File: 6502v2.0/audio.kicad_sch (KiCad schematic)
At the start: 24 parts, among them J16 AudioPlug4, U13 PSG_AY-3-8910, U14 PSG_AY-3-8910

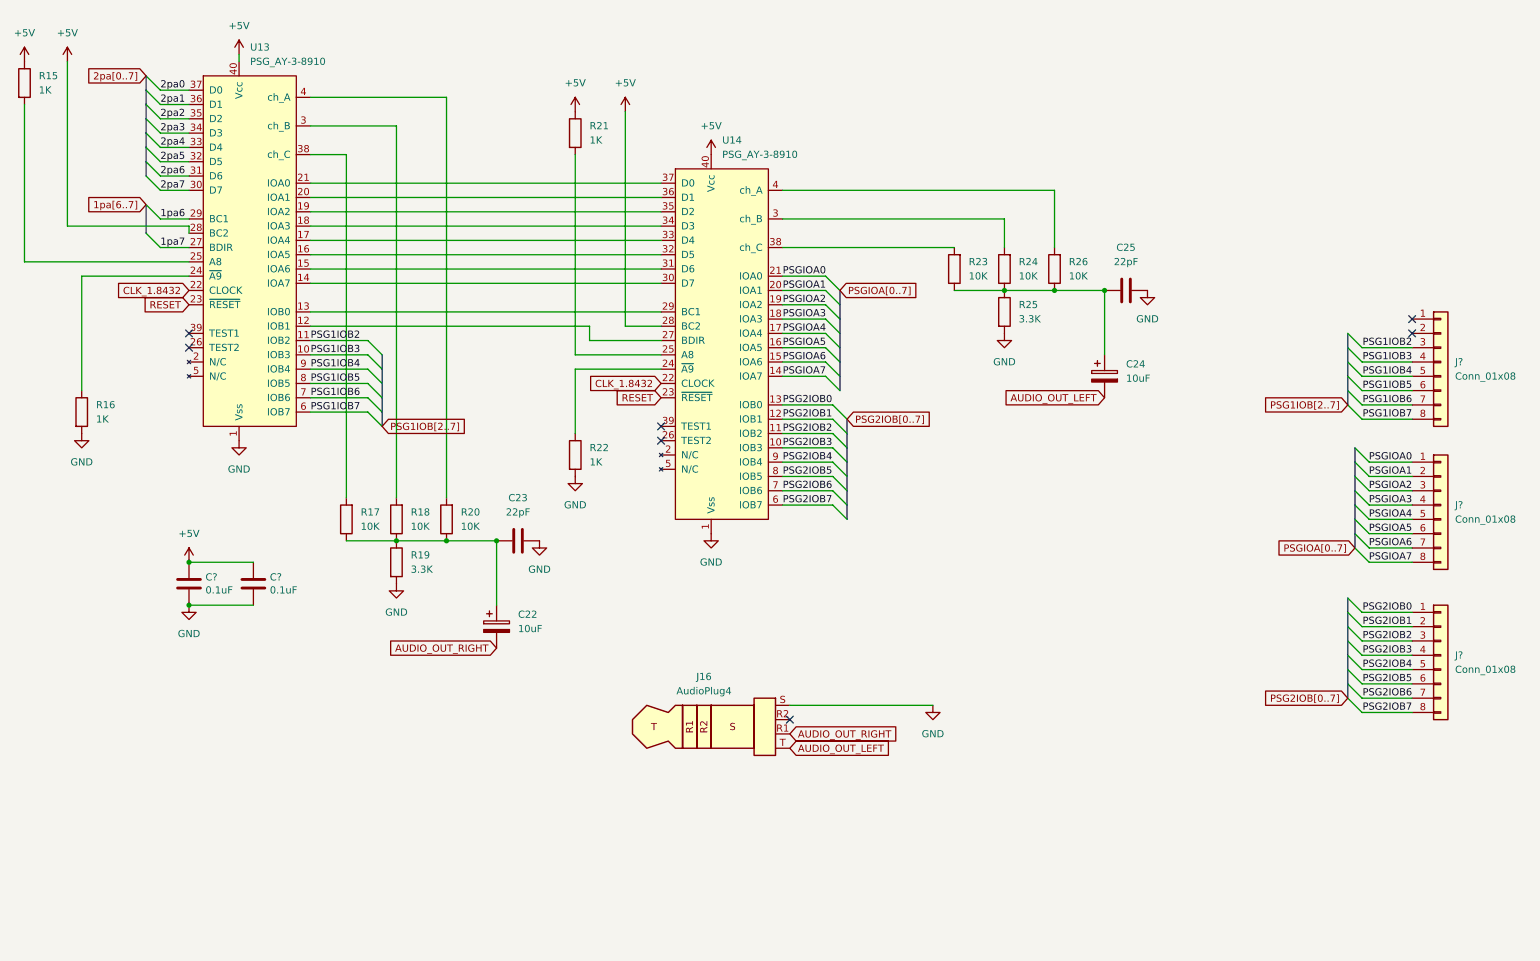
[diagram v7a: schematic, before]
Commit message: worked on new sound interface
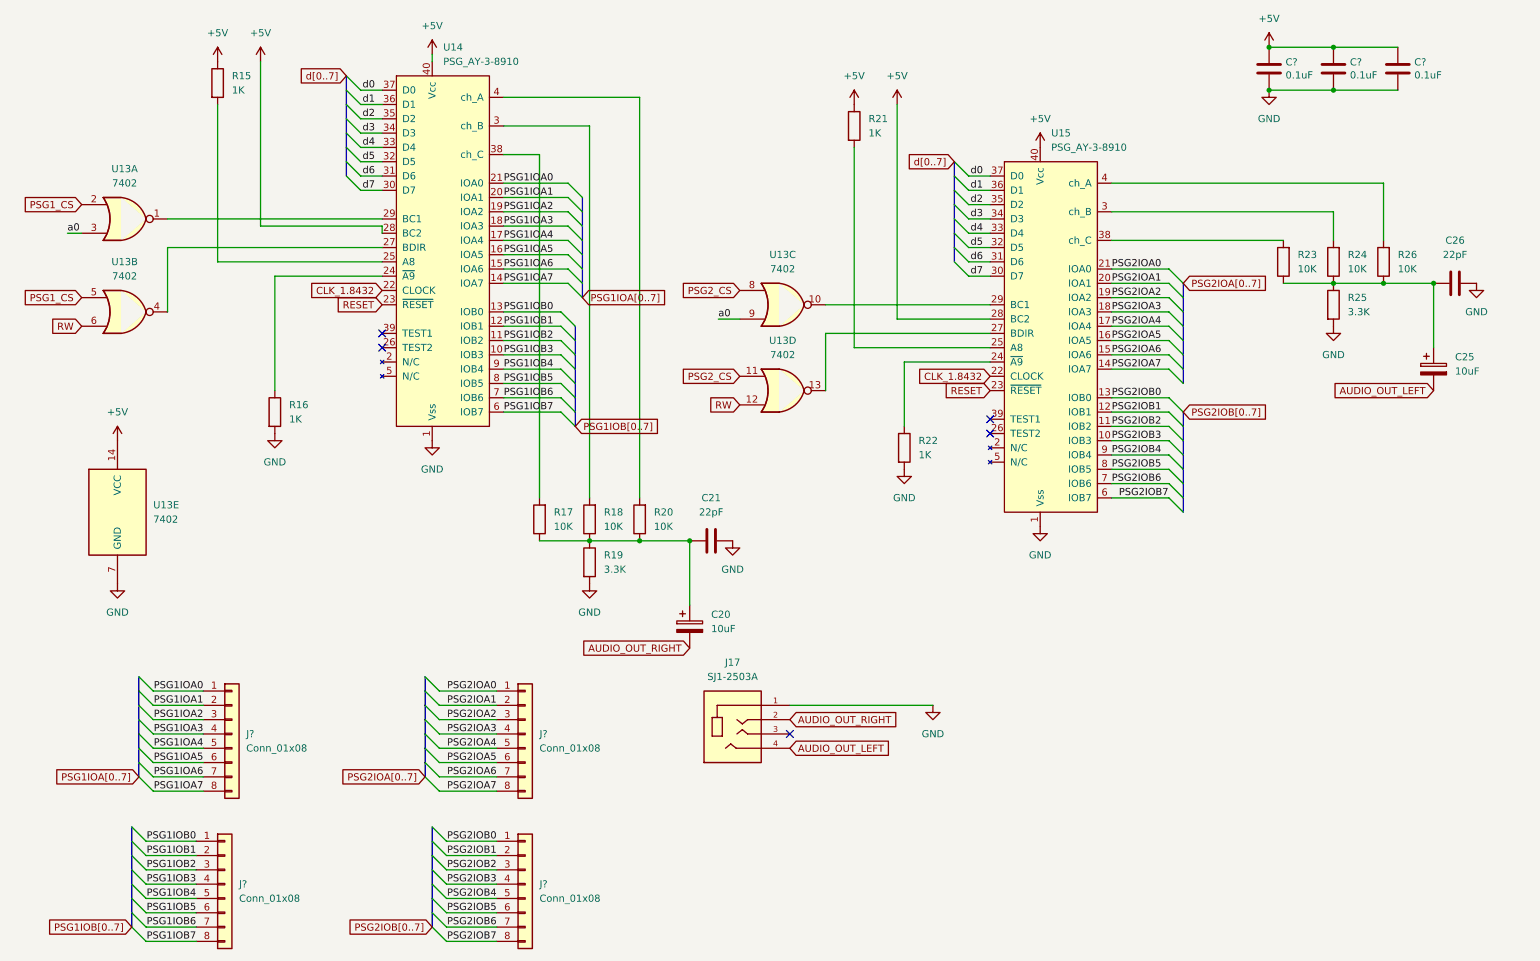
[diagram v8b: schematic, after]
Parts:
- removed J16: AudioPlug4, symbol Connector_Audio:AudioPlug4
- added C?: 0.1uF, Capacitor_THT:C_Disc_D5.1mm_W3.2mm_P5.00mm, symbol Device:C
- added J17: SJ1-2503A, symbol SJ1-2503A:SJ1-2503A
- added J?: Conn_01x08, Connector_PinHeader_2.54mm:PinHeader_1x08_P2.54mm_Vertical, symbol Connector_Generic:Conn_01x08
- added U13: 7402, Package_DIP:DIP-14_W7.62mm_Socket, symbol 74xx:7402
- renumbered C22 to C20, C23 to C21, C24 to C25, C25 to C26, U13 to U14, U14 to U15
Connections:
- net +5V: now also C?.1, U13.14 (VCC)
- net AUDIO_OUT_LEFT: now also J17.4
- net AUDIO_OUT_RIGHT: now also J17.2
- net GND: now also C?.2, J17.1, U13.7 (GND)
- net PSG1IOB0: now reaches J?.1 (Pin_1)
- net PSG1IOB0: now also U14.13 (IOB0)
- net PSG1IOB1: now reaches J?.2 (Pin_2)
- net PSG1IOB1: now also U14.12 (IOB1)
- net at U15.27 (BDIR): now also U13.13; no longer U14.12 (IOB1)
- net at U15.29 (BC1): now also U13.10; no longer U14.13 (IOB0)
- net PSG1IOA7: now reaches U14.14 (IOA7)
- net PSG1IOA7: now also J?.8 (Pin_8); no longer U15.30 (D7)
- net PSG1IOA6: now reaches U14.15 (IOA6)
- net PSG1IOA6: now also J?.7 (Pin_7); no longer U15.31 (D6)
- net PSG1IOA5: now reaches U14.16 (IOA5)
- net PSG1IOA5: now also J?.6 (Pin_6); no longer U15.32 (D5)
- net PSG1IOA4: now reaches U14.17 (IOA4)
- net PSG1IOA4: now also J?.5 (Pin_5); no longer U15.33 (D4)
- net PSG1IOA3: now reaches U14.18 (IOA3)
- net PSG1IOA3: now also J?.4 (Pin_4); no longer U15.34 (D3)
- net PSG1IOA2: now reaches U14.19 (IOA2)
- net PSG1IOA2: now also J?.3 (Pin_3); no longer U15.35 (D2)
- net PSG1IOA1: now reaches U14.20 (IOA1)
- net PSG1IOA1: now also J?.2 (Pin_2); no longer U15.36 (D1)
- net PSG1IOA0: now reaches U14.21 (IOA0)
- net PSG1IOA0: now also J?.1 (Pin_1); no longer U15.37 (D0)
- net 1pa6: no longer names the net of U14.29 (BC1)
- net 1pa6: now also U13.1
- net 1pa7: no longer names the net of U14.27 (BDIR)
- net 1pa7: now also U13.4
- net 2pa0 renamed d0
- net d0: now also U15.37 (D0)
- net 2pa1 renamed d1
- net d1: now also U15.36 (D1)
- net 2pa2 renamed d2
- net d2: now also U15.35 (D2)
- net 2pa3 renamed d3
- net d3: now also U15.34 (D3)
- net 2pa4 renamed d4
- net d4: now also U15.33 (D4)
- net 2pa5 renamed d5
- net d5: now also U15.32 (D5)
- net 2pa6 renamed d6
- net d6: now also U15.31 (D6)
- net 2pa7 renamed d7
- net d7: now also U15.30 (D7)
- net PSGIOA0 renamed PSG2IOA0
- net PSGIOA1 renamed PSG2IOA1
- net PSGIOA2 renamed PSG2IOA2
- net PSGIOA3 renamed PSG2IOA3
- net PSGIOA4 renamed PSG2IOA4
- net PSGIOA5 renamed PSG2IOA5
- net PSGIOA6 renamed PSG2IOA6
- net PSGIOA7 renamed PSG2IOA7
- new net PSG1_CS: U13.2, U13.5
- new net PSG2_CS: U13.11, U13.8
- new net RW: U13.12, U13.6
- new net a0: U13.3, U13.9
- no-connect marks 7 -> 5
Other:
- moved on the sheet: C20, C21, C25, C26, C?, J?, R15, R16, R17, R18, R19, R20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
